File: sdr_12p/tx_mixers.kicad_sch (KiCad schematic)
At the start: 0 parts

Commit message: basic arrangement of blocks
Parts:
- added U7: 74CBT1G125DBVRE4, DBV5, symbol SN74CBT1G125:74CBT1G125DBVRE4
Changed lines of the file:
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@@
 		(company "Andy McCann KA3KAF and Doug McCann KA3KAG")
 	)
+	(symbol
+		(lib_id "SN74CBT1G125:74CBT1G125DBVRE4")
+		(at 62.23 46.99 0)
+		(unit 1)
+		(exclude_from_sim no)
+		(in_bom yes)
+		(on_board yes)
+		(dnp no)
+		(fields_autoplaced yes)
+		(property "Reference" "U7"
+			(at 90.17 36.83 0)
+			(effects
+				(font
+					(size 1.524 1.524)
+				)
+			)
+		)
+		(property "Value" "74CBT1G125DBVRE4"
+			(at 90.17 39.37 0)
+			(effects
+				(font
+					(size 1.524 1.524)
+				)
+			)
+		)
+		(property "Footprint" "DBV5"
+			(at 62.23 46.99 0)
+			(effects
+				(font
+					(size 1.27 1.27)
+					(italic yes)
+				)
+				(hide yes)
+			)
+		)
+		(property "Datasheet" "https://www.ti.com/lit/gpn/sn74cbt1g125"
+			(at 62.23 46.99 0)
+			(effects
+				(font
+					(size 1.27 1.27)
+					(italic yes)
+				)
+				(hide yes)
+			)
+		)
+		(property "Description" ""
+			(at 62.23 46.99 0)
+			(effects
+				(font
+					(size 1.27 1.27)
+				)
+				(hide yes)
+			)
+		)
+		(pin "5"
+		)
+		(pin "4"
+		)
+		(pin "3"
+		)
+		(pin "2"
+		)
+		(pin "1"
+		)
+		(instances
+			(project ""
+				(path "/fe42ca2f-2bb8-4d5a-9e84-807788ed632f/bcf6c722-1668-4f59-9b47-5a2e203e881a"
+					(reference "U7")
+					(unit 1)
+				)
+			)
+		)
+	)
 )

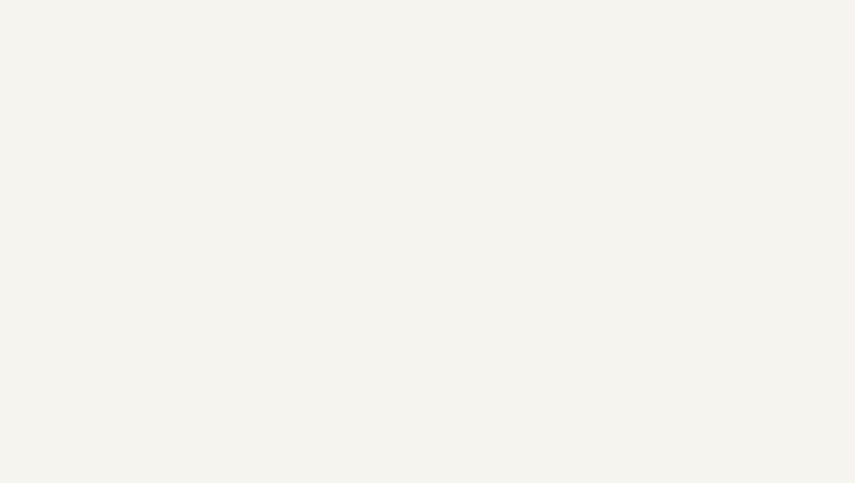
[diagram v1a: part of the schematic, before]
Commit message: added rx switches
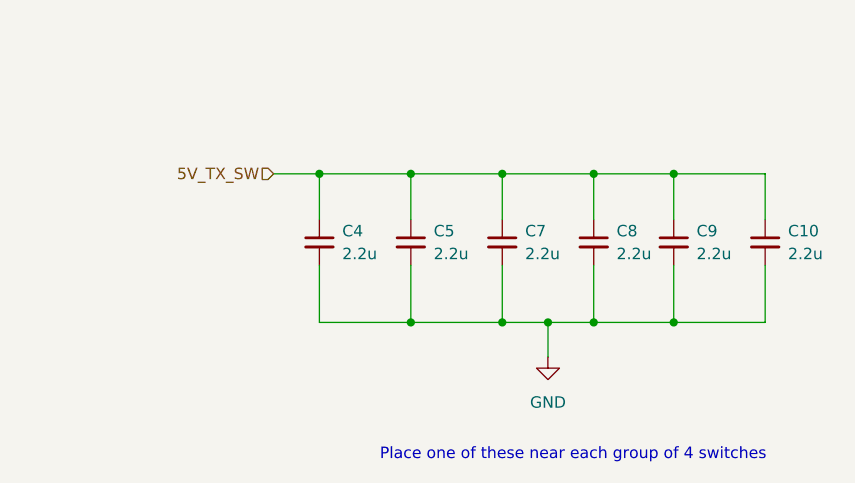
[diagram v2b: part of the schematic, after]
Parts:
- added C10, C4, C5, C7, C8, C9: 2.2u, symbol Device:C_Small
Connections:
- new net 5V_TX_SW: C10.1, C4.1, C5.1, C7.1, C8.1, C9.1
- new net GND: C10.2, C4.2, C5.2, C7.2, C8.2, C9.2
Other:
- note added: "Place one of these near each group of 4 switches"

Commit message: added Tx Mixer
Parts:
- added C100, C103, C104, C105, C106, C108, C82, C85, C86, C87, C88, C90, C91, C94, C95, C96, C97, C99: 0.1u, Resistor_SMD:R_0402_1005Metric_Pad0.72x0.64mm_HandSolder, symbol Device:C_Small
- added C109, C112, C113, C114, C115, C117: 2.2u, symbol Device:C_Small
- added U45, U46, U47, U48, U49, U50, U51, U52, U53, U54, U55, U56, U57, U58, U59, U60, U61, U62, U63, U64, U65, U66, U67: 74CBT1G125DBVRE4, DBV5, symbol SN74CBT1G125:74CBT1G125DBVRE4
- C10, C4, C5, C7, C8, C9: value 2.2u -> 0.1u; footprint (none) -> Resistor_SMD:R_0402_1005Metric_Pad0.72x0.64mm_HandSolder
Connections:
- net 5V_TX_SW: now also C109.1, C112.1, C113.1, C114.1, C115.1, C117.1; no longer C10.1, C4.1, C5.1, C7.1, C8.1, C9.1
- net GND: now also U7.3 (GND), C100.2, C103.2, C104.2, C105.2, C106.2, C108.2, C109.2, C112.2, C113.2, C114.2, C115.2, C117.2, C82.2, C85.2, C86.2, C87.2, C88.2, C90.2, C91.2, C94.2, C95.2, C96.2, C97.2, C99.2, U45.3 (GND), U46.3 (GND), U47.3 (GND), U48.3 (GND), U49.3 (GND), U50.3 (GND), U51.3 (GND), U52.3 (GND), U53.3 (GND), U54.3 (GND), U55.3 (GND), U56.3 (GND), U57.3 (GND), U58.3 (GND), U59.3 (GND), U60.3 (GND), U61.3 (GND), U62.3 (GND), U63.3 (GND), U64.3 (GND), U65.3 (GND), U66.3 (GND), U67.3 (GND)
- net CLK_P0+: now reaches U7.1 (*OE)
- net RF-: now reaches U7.2 (A)
- net RF-: now also U45.2 (A), U46.2 (A), U47.2 (A), U48.2 (A), U49.2 (A), U50.2 (A), U51.2 (A), U52.2 (A), U53.2 (A), U54.2 (A), U55.2 (A), U56.2 (A), U57.2 (A), U58.2 (A), U59.2 (A), U60.2 (A), U61.2 (A), U62.2 (A), U63.2 (A), U64.2 (A), U65.2 (A), U66.2 (A), U67.2 (A)
- net DAC_P0+: now reaches U7.4 (B)
- net 5V_TX_Mixer: now reaches U7.5 (VCC)
- net 5V_TX_Mixer: now also C10.1, C4.1, C5.1, C7.1, C8.1, C100.1, C103.1, C104.1, C105.1, C106.1, C108.1, C82.1, C85.1, C86.1, C87.1, C88.1, C90.1, C91.1, C94.1, C95.1, C96.1, C97.1, C99.1, U45.5 (VCC), U46.5 (VCC), U47.5 (VCC), U49.5 (VCC), U50.5 (VCC), U51.5 (VCC), U52.5 (VCC), U53.5 (VCC), U54.5 (VCC), U55.5 (VCC), U56.5 (VCC), U57.5 (VCC), U58.5 (VCC), U59.5 (VCC), U60.5 (VCC), U61.5 (VCC), U62.5 (VCC), U63.5 (VCC), U64.5 (VCC), U65.5 (VCC), U66.5 (VCC), U67.5 (VCC)
- new net: C9.1, U48.5 (VCC)
- new net CLK_P0-: U45.1 (*OE)
- new net CLK_P1+: U46.1 (*OE)
- new net CLK_P1-: U47.1 (*OE)
- new net CLK_P10+: U64.1 (*OE)
- new net CLK_P10-: U65.1 (*OE)
- new net CLK_P11+: U66.1 (*OE)
- new net CLK_P11-: U67.1 (*OE)
- new net CLK_P2+: U48.1 (*OE)
- new net CLK_P2-: U49.1 (*OE)
- new net CLK_P3+: U50.1 (*OE)
- new net CLK_P3-: U51.1 (*OE)
- new net CLK_P4+: U52.1 (*OE)
- new net CLK_P4-: U53.1 (*OE)
- new net CLK_P5+: U54.1 (*OE)
- new net CLK_P5-: U55.1 (*OE)
- new net CLK_P6+: U56.1 (*OE)
- new net CLK_P6-: U57.1 (*OE)
- new net CLK_P7+: U58.1 (*OE)
- new net CLK_P7-: U59.1 (*OE)
- new net CLK_P8+: U60.1 (*OE)
- new net CLK_P8-: U61.1 (*OE)
- new net CLK_P9+: U62.1 (*OE)
- new net CLK_P9-: U63.1 (*OE)
- new net DAC_P0-: U45.4 (B)
- new net DAC_P1+: U46.4 (B)
- new net DAC_P1-: U47.4 (B)
- new net DAC_P10+: U64.4 (B)
- new net DAC_P10-: U65.4 (B)
- new net DAC_P11+: U66.4 (B)
- new net DAC_P11-: U67.4 (B)
- new net DAC_P2+: U48.4 (B)
- new net DAC_P2-: U49.4 (B)
- new net DAC_P3+: U50.4 (B)
- new net DAC_P3-: U51.4 (B)
- new net DAC_P4+: U52.4 (B)
- new net DAC_P4-: U53.4 (B)
- new net DAC_P5+: U54.4 (B)
- new net DAC_P5-: U55.4 (B)
- new net DAC_P6+: U56.4 (B)
- new net DAC_P6-: U57.4 (B)
- new net DAC_P7+: U58.4 (B)
- new net DAC_P7-: U59.4 (B)
- new net DAC_P8+: U60.4 (B)
- new net DAC_P8-: U61.4 (B)
- new net DAC_P9+: U62.4 (B)
- new net DAC_P9-: U63.4 (B)
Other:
- note added: "0402 0.1u caps need to be placed right at VCC pin with no trace to ground (use via)"
